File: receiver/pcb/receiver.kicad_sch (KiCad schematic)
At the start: 27 parts, among them J4 Conn_01x01_Female-weapon, J5 Conn_01x01_Female-weapon, M1 Conn_01x02_Female, M2 Conn_01x02_Female, U1 DRV8870DDA, U2 DRV8870DDA, U3 AMS1117-3.3, U4 ESP32-C3-MINI-1

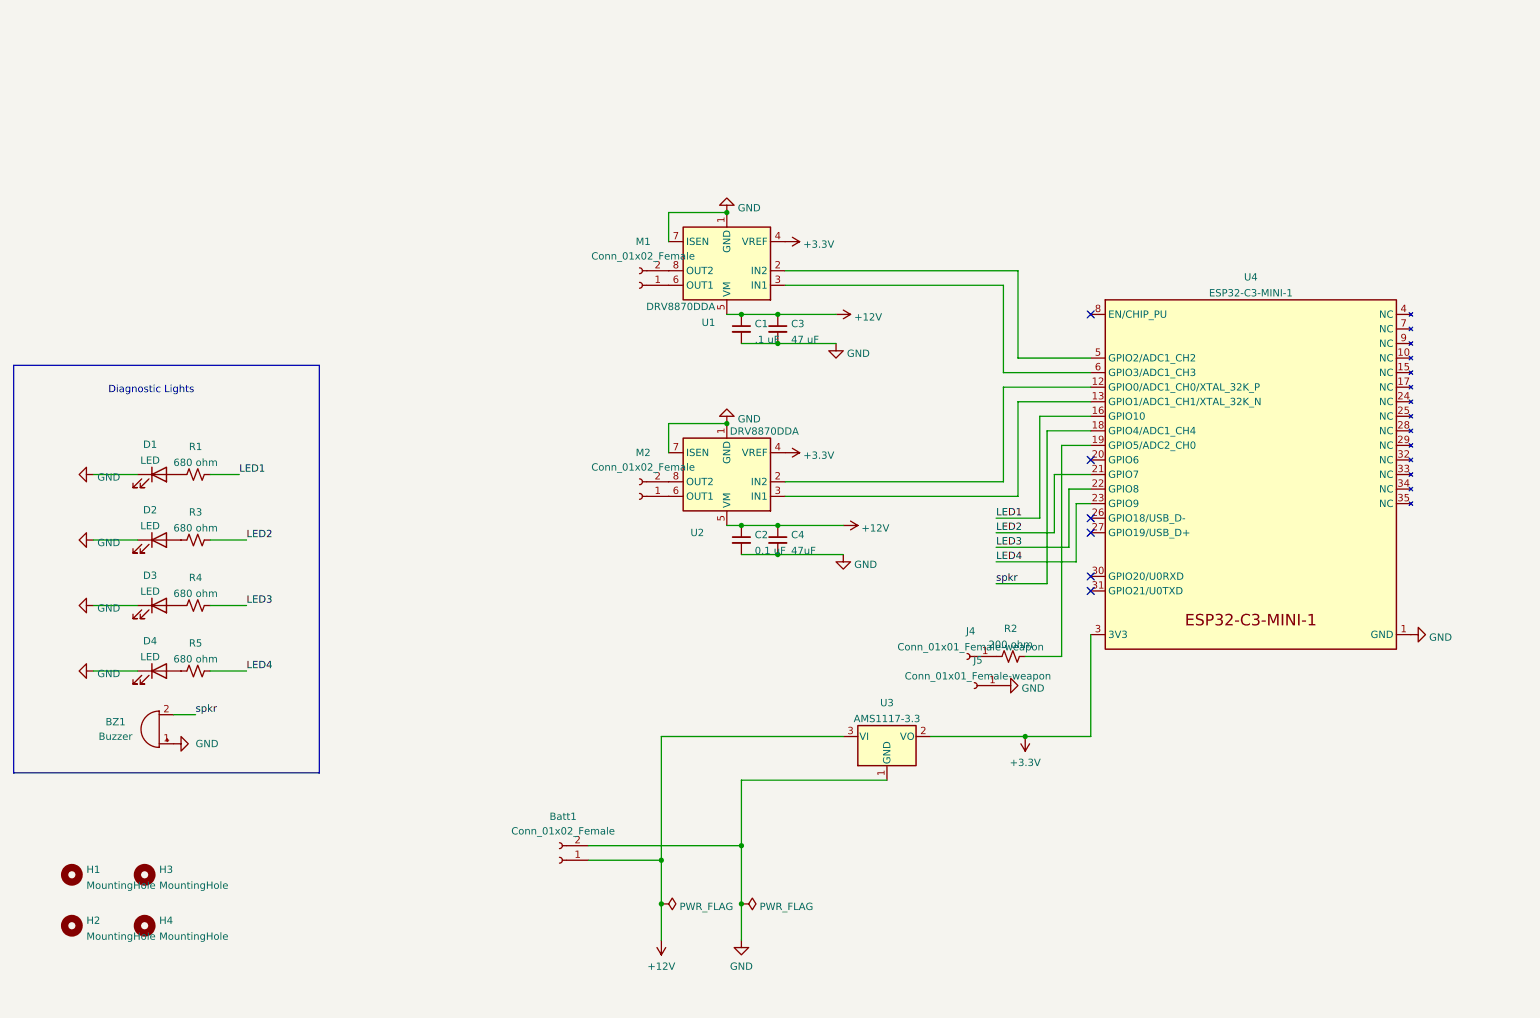
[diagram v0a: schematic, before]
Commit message: added footprints library
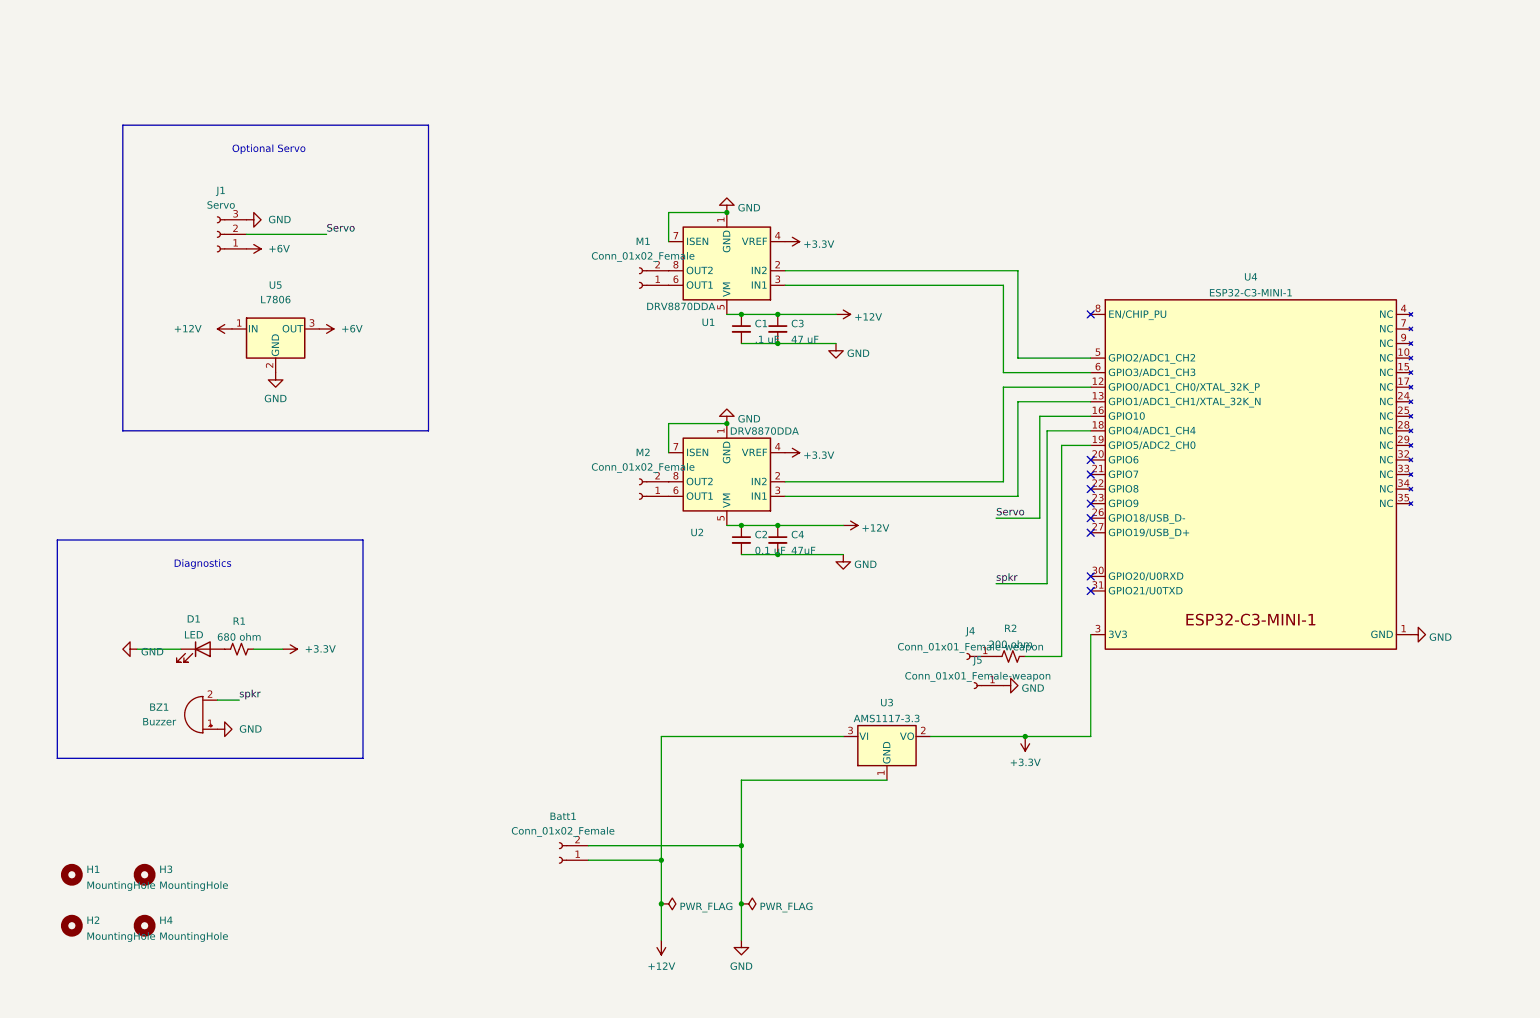
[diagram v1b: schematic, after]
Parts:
- removed D2, D3, D4: LED, LED_SMD:LED_0805_2012Metric_Pad1.15x1.40mm_HandSolder, symbol Device:LED
- removed R3, R4, R5: 680 ohm, Resistor_SMD:R_0805_2012Metric_Pad1.20x1.40mm_HandSolder, symbol Device:R_Small_US
- added J1: Servo, Connector_PinSocket_2.54mm:PinSocket_1x03_P2.54mm_Vertical, symbol Connector:Conn_01x03_Female
- added U5: L7806, Package_TO_SOT_SMD:TO-252-3_TabPin2, symbol Regulator_Linear:L7806
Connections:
- net +12V: now also U5.1 (IN)
- net +3V3: now also R1.1
- net GND: now also J1.3 (Pin_3), U5.2 (GND)
- net LED1 renamed Servo
- net Servo: now also J1.2 (Pin_2); no longer R1.1
- net LED2: no longer names the net of U4.21 (GPIO7)
- net LED3: no longer names the net of U4.22 (GPIO8)
- net LED4: no longer names the net of U4.23 (GPIO9)
- new net +6V: J1.1 (Pin_1), U5.3 (OUT)
- no-connect marks 6 -> 9
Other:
- note added: "Diagnostics"
- note added: "Optional Servo"
- note removed: "Diagnostic Lights"
- moved on the sheet: BZ1, D1, R1

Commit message: change ESC connection to 3pin header
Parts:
- removed J4, J5: Conn_01x01_Female-weapon, Connector_PinSocket_2.54mm:PinSocket_1x01_P2.54mm_Vertical, symbol Connector:Conn_01x01_Female
- added ESC1: ESC, Connector_PinSocket_2.54mm:PinSocket_1x03_P2.54mm_Vertical, symbol Connector:Conn_01x03_Female
- renumbered U3 to AMS1117, U4 to ESP32-C3, U5 to L7806, D1 to PWR1, R1 to R680, J1 to Servo1
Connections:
- net GND: now also ESC1.1 (Pin_1)
- net at R2.2: now also ESC1.3 (Pin_3)
- no-connect marks 9 -> 10
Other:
- moved on the sheet: R2

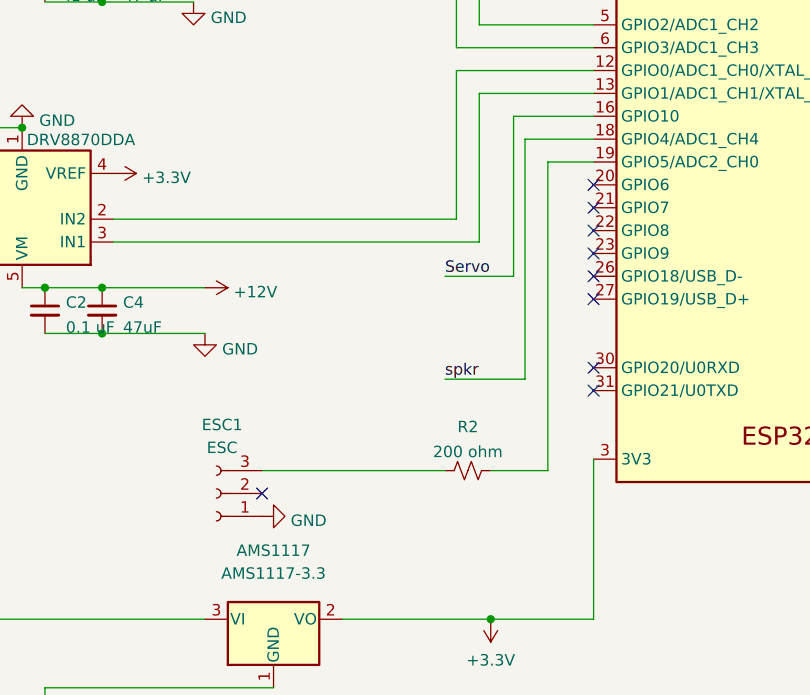
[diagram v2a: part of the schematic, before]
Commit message: made square pin consistently more positive voltage
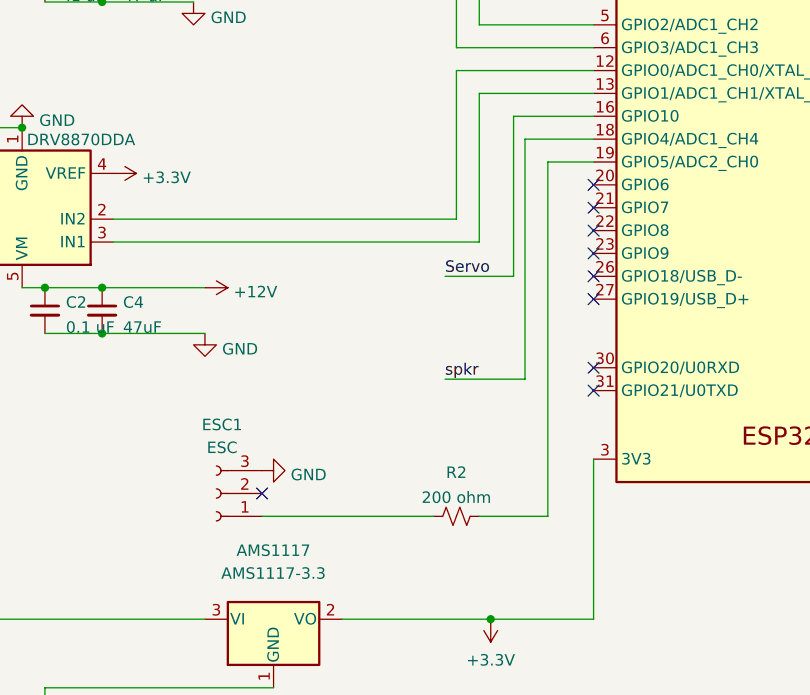
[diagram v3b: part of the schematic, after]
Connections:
- net GND: now also ESC1.3 (Pin_3); no longer ESC1.1 (Pin_1)
- net at R2.2: now also ESC1.1 (Pin_1); no longer ESC1.3 (Pin_3)
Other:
- moved on the sheet: R2
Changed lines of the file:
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@@
     (stroke (width 0) (type default) (color 0 0 0 0))
   )
-  (wire (pts (xy 194.31 125.73) (xy 200.66 125.73))
+  (wire (pts (xy 193.04 130.81) (xy 200.66 130.81))
     (stroke (width 0) (type default) (color 0 0 0 0))
   )
@@
     (stroke (width 0) (type default) (color 0 0 0 0))
   )
-  (wire (pts (xy 168.91 125.73) (xy 189.23 125.73))
-    (stroke (width 0) (type default) (color 0 0 0 0))
-  )
   (wire (pts (xy 118.11 163.83) (xy 130.81 163.83))
     (stroke (width 0) (type default) (color 0 0 0 0))
@@
     (stroke (width 0) (type default) (color 0 0 0 0))
   )
-  (wire (pts (xy 200.66 91.44) (xy 200.66 125.73))
+  (wire (pts (xy 200.66 91.44) (xy 200.66 130.81))
     (stroke (width 0) (type default) (color 0 0 0 0))
   )
@@
   )
   (wire (pts (xy 132.08 87.63) (xy 132.08 92.71))
+    (stroke (width 0) (type default) (color 0 0 0 0))
+  )
+  (wire (pts (xy 168.91 130.81) (xy 187.96 130.81))
     (stroke (width 0) (type default) (color 0 0 0 0))
   )
@@
     (pin "1")
   )
-  (symbol (lib_id "Device:R_Small_US") (at 191.77 125.73 270) (unit 1)
-    (in_bom yes) (on_board yes) (fields_autoplaced)
-    (property "Reference" "R2" (id 0) (at 191.77 120.8745 90))
-    (property "Value" "200 ohm" (id 1) (at 191.77 123.6496 90))
-    (property "Footprint" "Resistor_SMD:R_0805_2012Metric_Pad1.20x1.40mm_HandSolder" (id 2) (at 191.77 125.73 0)
-      (effects (font (size 1.27 1.27)) hide)
-    )
-    (property "Datasheet" "~" (id 3) (at 191.77 125.73 0)
+  (symbol (lib_id "Device:R_Small_US") (at 190.5 130.81 270) (unit 1)
+    (in_bom yes) (on_board yes) (fields_autoplaced)
+    (property "Reference" "R2" (id 0) (at 190.5 125.9545 90))
+    (property "Value" "200 ohm" (id 1) (at 190.5 128.7296 90))
+    (property "Footprint" "Resistor_SMD:R_0805_2012Metric_Pad1.20x1.40mm_HandSolder" (id 2) (at 190.5 130.81 0)
+      (effects (font (size 1.27 1.27)) hide)
+    )
+    (property "Datasheet" "~" (id 3) (at 190.5 130.81 0)
       (effects (font (size 1.27 1.27)) hide)
     )
@@
     (pin "2")
   )
-  (symbol (lib_id "power:GND") (at 168.91 130.81 90) (unit 1)
-    (in_bom yes) (on_board yes) (fields_autoplaced)
-    (property "Reference" "#PWR014" (id 0) (at 175.26 130.81 0)
-      (effects (font (size 1.27 1.27)) hide)
-    )
-    (property "Value" "GND" (id 1) (at 172.085 131.289 90)
+  (symbol (lib_id "power:GND") (at 168.91 125.73 90) (unit 1)
+    (in_bom yes) (on_board yes) (fields_autoplaced)
+    (property "Reference" "#PWR014" (id 0) (at 175.26 125.73 0)
+      (effects (font (size 1.27 1.27)) hide)
+    )
+    (property "Value" "GND" (id 1) (at 172.085 126.209 90)
       (effects (font (size 1.27 1.27)) (justify right))
     )
-    (property "Footprint" "" (id 2) (at 168.91 130.81 0)
-      (effects (font (size 1.27 1.27)) hide)
-    )
-    (property "Datasheet" "" (id 3) (at 168.91 130.81 0)
-      (effects (font (size 1.27 1.27)) hide)
-    )
+    (property "Footprint" "" (id 2) (at 168.91 125.73 0)
+      (effects (font (size 1.27 1.27)) hide)
+    )
+    (property "Datasheet" "" (id 3) (at 168.91 125.73 0)
+      (effects (font (size 1.27 1.27)) hide)
+    )

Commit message: V3 of receiver as ordered.
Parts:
- removed R2: 200 ohm, Resistor_SMD:R_0805_2012Metric_Pad1.20x1.40mm_HandSolder, symbol Device:R_Small_US
- added R1: 10k, Resistor_SMD:R_0805_2012Metric_Pad1.20x1.40mm_HandSolder, symbol Device:R_Small_US
- Batt1: footprint Connector_PinSocket_2.54mm:PinSocket_1x02_P2.54mm_Vertical -> battery:battery_pads
- renumbered PWR1 to LED1, R680 to R2
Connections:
- net +6V: now also Servo1.2 (Pin_2); no longer Servo1.1 (Pin_1)
- net GND: now also R1.1
- net Servo: now also Servo1.1 (Pin_1); no longer Servo1.2 (Pin_2)
- net at ESC1.1 (Pin_1): now also ESP32-C3.19 (GPIO5/ADC2_CH0), R1.2

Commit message: receiver V4 ordered
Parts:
- removed AMS1117: AMS1117-3.3, Package_TO_SOT_SMD:SOT-223-3_TabPin2, symbol Regulator_Linear:AMS1117-3.3
- removed BZ1: Buzzer, Buzzer_Beeper:Buzzer_CUI_CPT-9019S-SMT, symbol Device:Buzzer
- removed C3: 47 uF, Capacitor_SMD:C_0805_2012Metric_Pad1.18x1.45mm_HandSolder, symbol Device:C_Small
- removed C4: 47uF, Capacitor_SMD:C_0805_2012Metric_Pad1.18x1.45mm_HandSolder, symbol Device:C_Small
- removed M1, M2: Conn_01x02_Female, Connector_PinSocket_2.54mm:PinSocket_1x02_P2.54mm_Vertical, symbol Connector:Conn_01x02_Female
- removed U1, U2: DRV8870DDA, Package_SO:Texas_HTSOP-8-1EP_3.9x4.9mm_P1.27mm_EP2.95x4.9mm_Mask2.4x3.1mm_ThermalVias, symbol Driver_Motor:DRV8870DDA
- added C5: .1 uF, Capacitor_SMD:C_0805_2012Metric_Pad1.18x1.45mm_HandSolder, symbol Device:C_Small
- added C6: 47 uF, Capacitor_SMD:C_0805_2012Metric_Pad1.18x1.45mm_HandSolder, symbol Device:C_Small
- added Comms1: LED, LED_SMD:LED_0805_2012Metric_Pad1.15x1.40mm_HandSolder, symbol Device:LED
- added IC1, IC2: DRV8251DDAR, drv8251:SOIC127P600X170-9N, symbol DRV8251:DRV8251DDAR
- added ML1, MR1: Conn_01x02_Female, Connector_PinSocket_2.54mm:PinSocket_1x02_P2.54mm_Vertical, symbol Connector:Conn_01x02_Female
- added PS1: UA78M33CDCYRG3, ua78-vreg:SOT230P700X180-4N, symbol libraries:UA78M33CDCYRG3
- added R3: 680 ohm, Resistor_SMD:R_0805_2012Metric_Pad1.20x1.40mm_HandSolder, symbol Device:R_Small_US
- C1: value .1 uF -> 47 uF
- C2: value 0.1 uF -> .1 uF
- renumbered LED1 to PWR1
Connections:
- net +12V: now also C5.1, C6.1, IC1.5 (VM), IC2.5 (VM), PS1.1 (INPUT)
- net +3V3: now also IC1.4 (VREF), IC2.4 (VREF), PS1.3 (OUTPUT); no longer R2.1
- net GND: now also C5.2, C6.2, Comms1.1 (K), IC1.1 (GND), IC1.7 (ISEN), IC1.9 (THERMAL_PAD), IC2.1 (GND), IC2.7 (ISEN), IC2.9 (THERMAL_PAD), PS1.2 (COMMON_1), PS1.4 (COMMON_2)
- net at ESP32-C3.12 (GPIO0/ADC1_CH0/XTAL_32K_P): now also IC2.3 (IN1)
- net at ESP32-C3.13 (GPIO1/ADC1_CH1/XTAL_32K_N): now also IC2.2 (IN2)
- net comms: now reaches ESP32-C3.20 (GPIO6)
- net comms: now also R3.1
- net at ESP32-C3.5 (GPIO2/ADC1_CH2): now also IC1.3 (IN1)
- net at ESP32-C3.6 (GPIO3/ADC1_CH3): now also IC1.2 (IN2)
- net spkr renamed pwr
- net pwr: now also R2.1
- new net: Comms1.2 (A), R3.2
- new net: IC1.8 (OUT2), ML1.1 (Pin_1)
- new net: IC1.6 (OUT1), ML1.2 (Pin_2)
- new net: IC2.6 (OUT1), MR1.2 (Pin_2)
- new net: IC2.8 (OUT2), MR1.1 (Pin_1)
- no-connect marks 10 -> 9
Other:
- moved on the sheet: Batt1, ESC1, ESP32-C3, L7806, PWR1, R1, R2, Servo1
